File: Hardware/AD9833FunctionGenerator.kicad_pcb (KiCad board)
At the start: 2 copper layers, 125.7 x 114.3 mm, 54 parts, among them U1 LM7805_TO220

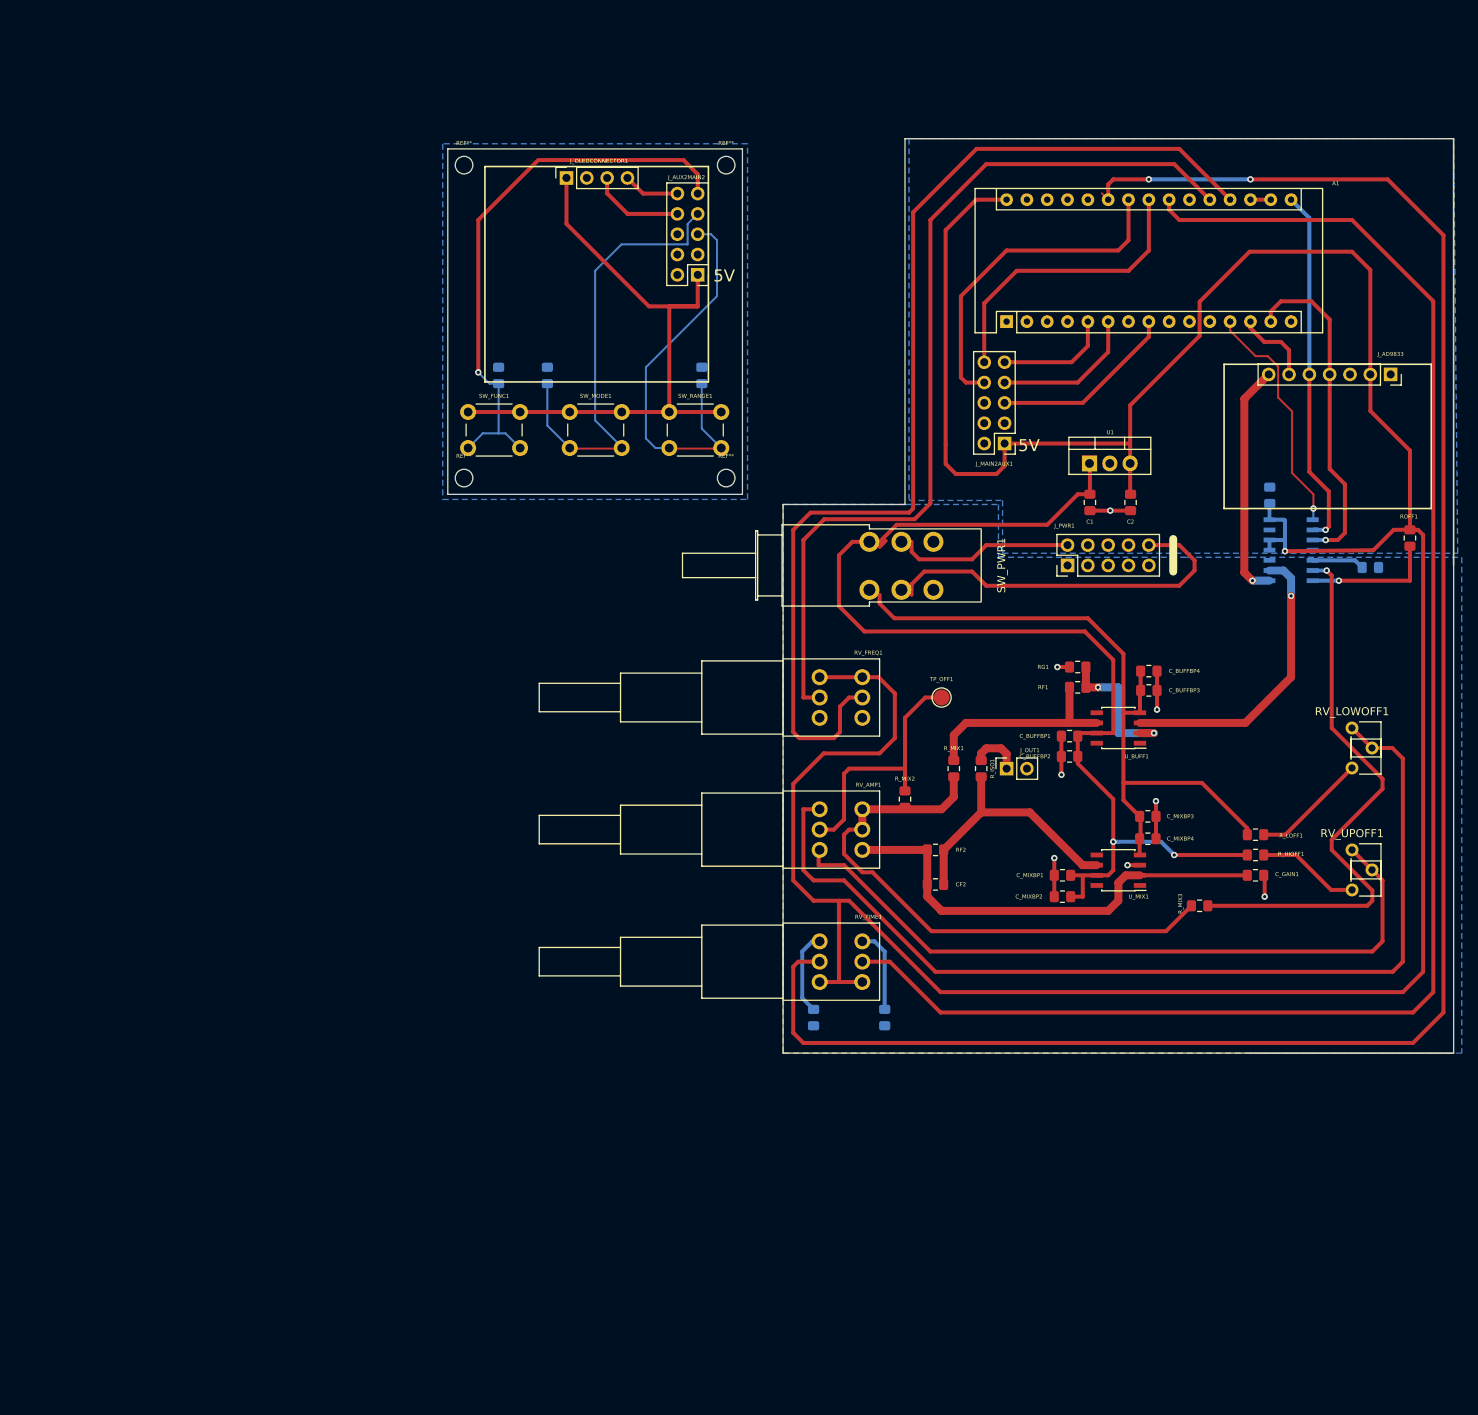
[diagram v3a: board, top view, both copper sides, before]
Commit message: increased size of board layout to accomodate pot clearance.
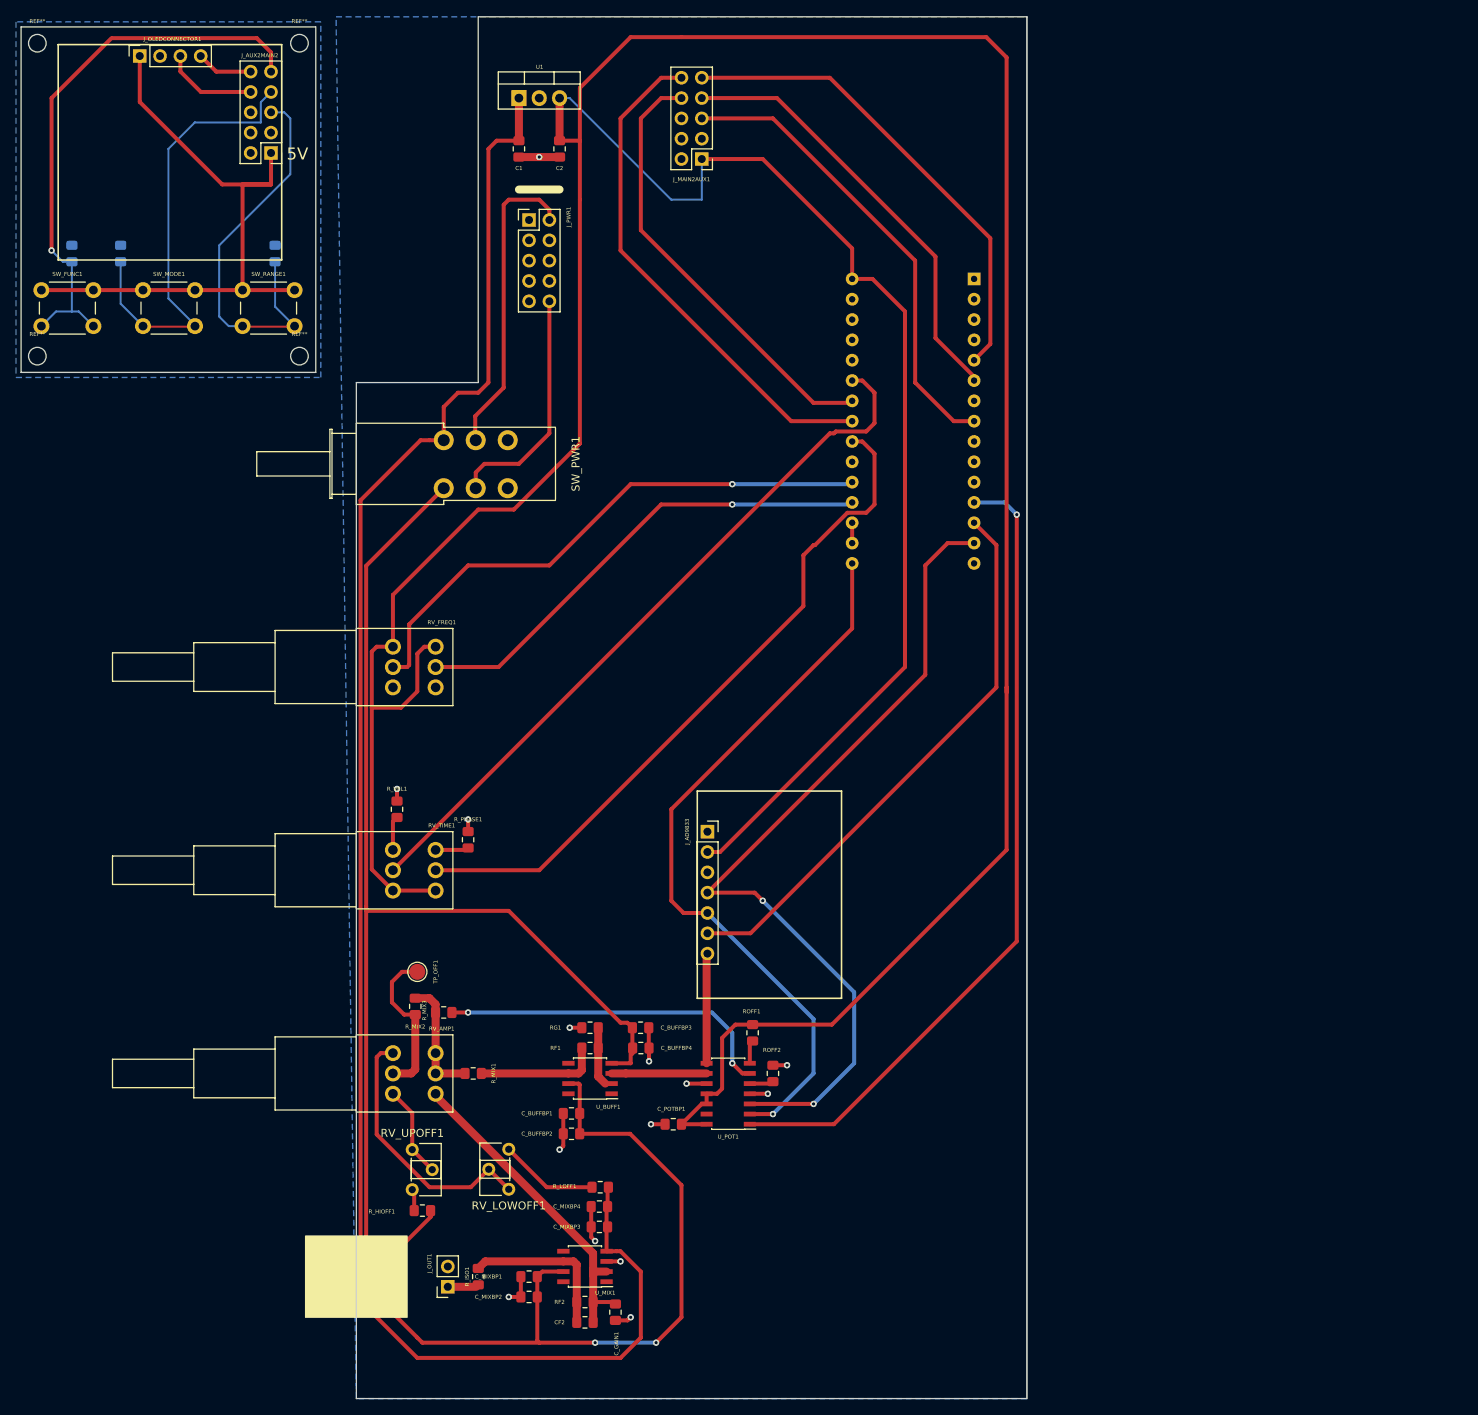
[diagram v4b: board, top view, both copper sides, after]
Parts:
- A1: moved to B.Cu
- C_POTBP1, ROFF2, R_PHASE1, R_VEL1, U_POT1: moved to F.Cu
- moved RV_UPOFF1 123.3 mm to (73.0, 161.9)
- moved RV_LOWOFF1 120.1 mm to (85.1, 166.9), turned to 180 degrees
- moved R_HIOFF1 113.2 mm to (74.3, 169.5), turned to 180 degrees
- moved C_POTBP1 108.3 mm to (105.7, 158.8), turned to 180 degrees
- moved ROFF1 102.8 mm to (115.6, 147.3)
- moved J_AD9833 102.8 mm to (109.9, 122.2), turned to 0 degrees
- moved ROFF2 97.9 mm to (118.1, 152.4), turned to 90 degrees
- moved U_POT1 97.8 mm to (112.5, 154.9)
- moved C_GAIN1 96.9 mm to (98.4, 182.2), turned to 270 degrees
- moved R_MIX3 95.4 mm to (77.0, 144.8)
- moved J_OUT1 95.3 mm to (77.5, 179.1), turned to 180 degrees
- moved R_LOFF1 93.0 mm to (96.5, 166.6), turned to 180 degrees
- moved R_ISO1 89.4 mm to (81.3, 177.8), turned to 90 degrees
- moved C_MIXBP3 85.6 mm to (96.4, 171.6), turned to 180 degrees
- moved U1 84.7 mm to (86.4, 30.5)
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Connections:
- C_BUFFBP1 pad 2: /AGND -> /GND
- C_BUFFBP2 pad 2: /AGND -> /GND
- C_BUFFBP3 pad 2: /AGND -> /GND
- C_BUFFBP4 pad 2: /AGND -> /GND
- C_GAIN1 pad 2: /AGND -> /GND
- C_MIXBP1 pad 2: /AGND -> /GND
- C_MIXBP2 pad 2: /AGND -> /GND
- C_MIXBP3 pad 2: /AGND -> /GND
- C_MIXBP4 pad 2: /AGND -> /GND
- J_OUT1 pad 2: /AGND -> /GND
- J_PWR1 pad 3: /AGND -> (no net)
- J_PWR1 pad 5: /AGND -> (no net)
- J_PWR1 pad 7: /AGND -> (no net)
- RG1 pad 1: /AGND -> /GND
- ROFF2 pad 2: /AGND -> /GND
- RV_FREQ1 pad 1: /AGND -> /GND
- RV_FREQ1 pad 4: /AGND -> /GND
- R_PHASE1 pad 1: /AGND -> /GND
- R_VEL1 pad 1: /AGND -> /GND
- U_MIX1 pad 3: /AGND -> /GND
- U_POT1 pad 10: /AGND -> /GND
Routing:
- net /VEL1: track 241.0 -> 90.6 mm, vias 2 -> 0
- net /-12V: track 86.0 -> 213.3 mm, vias 0 -> 2
- net /+12V: track 142.8 -> 268.1 mm
- net /5V: track 382.3 -> 505.0 mm, vias 1 -> 0
- net /PHASE1: track 200.2 -> 87.3 mm
- net Net-(RV_AMP1-Pad3): track 124.2 -> 33.1 mm
- net Net-(RV_AMP1-Pad1): track 90.4 -> 11.5 mm
- net /FREQHI: track 136.5 -> 60.6 mm, vias 0 -> 1
- net /POT_CS: track 30.0 -> 102.1 mm
- net /MOSI: track 42.0 -> 107.0 mm, vias 1 -> 2
- net /DDS_CS: track 9.82 -> 70.6 mm
- net Net-(RV_AMP1-Pad5): track 70.8 -> 15.2 mm
- net /SCK: track 45.0 -> 92.3 mm
- net /WAVEBTN: track 13.8 -> 60.5 mm
- net /FREQLO: track 114.5 -> 70.0 mm, vias 0 -> 1
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- removed copper zone on B.Cu, net /AGND
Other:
- board size 125.7 x 114.3 mm -> 125.7 x 172.7 mm
- board text added: "GAP"
